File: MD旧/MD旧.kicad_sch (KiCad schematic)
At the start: 42 parts, among them J1 Conn_01x04_Pin, J2 Conn_02x04_Odd_Even, J3 XT60-M, J4 XT60-M

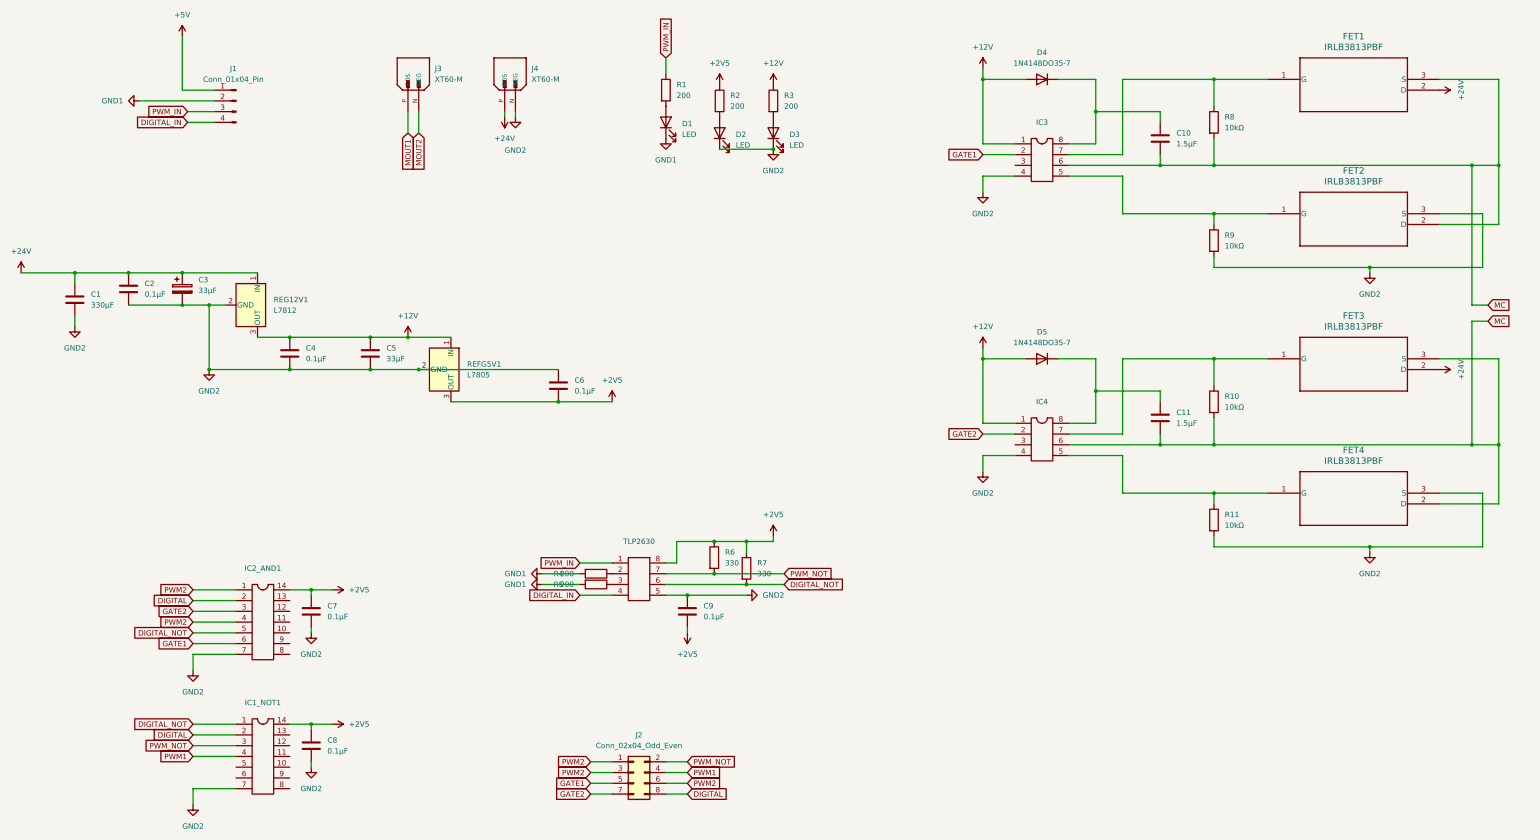
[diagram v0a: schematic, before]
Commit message: 回路図にわかりやすくテキスト入れただけでPCB側の変更はしてないです
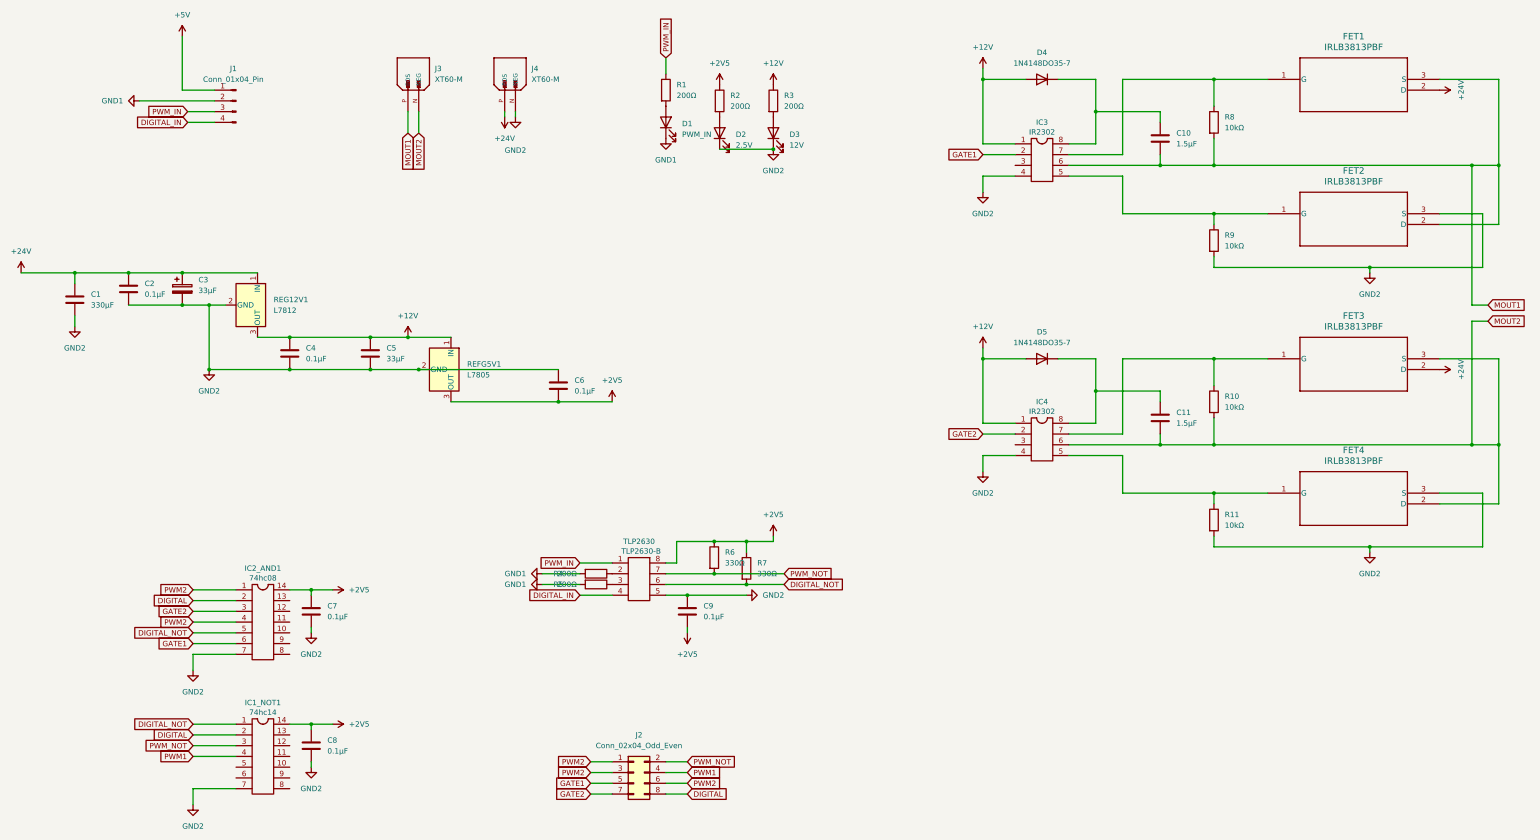
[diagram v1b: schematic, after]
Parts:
- D1: value LED -> PWM_IN
- D2: value LED -> 2.5V
- D3: value LED -> 12V
- R1, R3, R4, R5: value 200 -> 200Ω
- R2: value 200 -> 200Ω
- R6, R7: value 330 -> 330Ω
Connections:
- net MOUT1: now also C10.2, FET1.3 (S), FET2.2 (D), IC3.6, R8.2
- net MOUT2: now also C11.2, FET3.3 (S), FET4.2 (D), IC4.6, R10.2
- removed net MC: C10.2, C11.2, FET1.3 (S), FET2.2 (D), FET3.3 (S), FET4.2 (D), IC3.6, IC4.6, R10.2, R8.2
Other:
- note added: "74hc08"
- note added: "74hc14"
- note added: "IR2302"
- note added: "TLP2630-B"
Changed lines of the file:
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@@
 	(generator_version "9.0")
 	(paper "A3")
+	(text "74hc14"
+		(exclude_from_sim no)
+		(at 82.55 218.44 0)
+		(effects
+			(font
+				(size 1.27 1.27)
+			)
+		)
+	)
+	(text "IR2302"
+		(exclude_from_sim no)
+		(at 266.7 147.32 0)
+		(effects
+			(font
+				(size 1.27 1.27)
+			)
+		)
+	)
+	(text "TLP2630-B"
+		(exclude_from_sim no)
+		(at 171.958 180.34 0)
+		(effects
+			(font
+				(size 1.27 1.27)
+			)
+		)
+	)
+	(text "74hc08"
+		(exclude_from_sim no)
+		(at 82.55 186.69 0)
+		(effects
+			(font
+				(size 1.27 1.27)
+			)
+		)
+	)
+	(text "IR2302"
+		(exclude_from_sim no)
+		(at 266.7 81.28 0)
+		(effects
+			(font
+				(size 1.27 1.27)
+			)
+		)
+	)
 	(junction
 		(at 374.65 88.9)
@@
 		)
 	)
-	(global_label "MC"
+	(global_label "MOUT2"
 		(shape input)
 		(at 372.11 125.73 0)
@@
 		)
 		(property "Intersheetrefs" "${INTERSHEET_REFS}"
-			(at 377.8166 125.73 0)
+			(at 381.3847 125.73 0)
 			(effects
 				(font
@@
 		)
 	)
-	(global_label "MC"
+	(global_label "MOUT1"
 		(shape input)
 		(at 372.11 121.92 0)
@@
 		)
 		(property "Intersheetrefs" "${INTERSHEET_REFS}"
-			(at 377.8166 121.92 0)
+			(at 381.3847 121.92 0)
 			(effects
 				(font
@@
 			)
 		)
-		(property "Value" "200"
+		(property "Value" "200Ω"
 			(at 154.432 185.42 90)
 			(effects
@@
 			)
 		)
-		(property "Value" "LED"
+		(property "Value" "PWM_IN"
 			(at 181.61 81.5974 90)
 			(effects
@@
 			)
 		)
-		(property "Value" "LED"
+		(property "Value" "2.5V"
 			(at 194.31 84.1374 90)
 			(effects
@@
 			)
 		)
-		(property "Value" "200"
+		(property "Value" "200Ω"
 			(at 180.34 72.3899 0)
 			(effects
@@
 			)
 		)
-		(property "Value" "200"
+		(property "Value" "200Ω"
 			(at 154.432 187.96 90)
 			(effects
@@
 			)
 		)
-		(property "Value" "330"
+		(property "Value" "330Ω"
 			(at 199.39 185.4199 0)
 			(effects
@@
 			)
 		)
-		(property "Value" "200"
+		(property "Value" "200Ω"
 			(at 193.04 74.9299 0)
 			(effects
@@
 			)
 		)
-		(property "Value" "LED"
+		(property "Value" "12V"
 			(at 207.01 84.1374 90)
 			(effects
@@
 			)
 		)
-		(property "Value" "330"
+		(property "Value" "330Ω"
 			(at 191.77 182.8799 0)
 			(effects
@@
 			)
 		)
-		(property "Value" "200"
+		(property "Value" "200Ω"
 			(at 205.74 74.9299 0)
 			(effects
